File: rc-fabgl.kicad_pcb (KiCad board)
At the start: 2 copper layers, 99.1 x 49.9 mm, 45 parts, among them J1 RC2014, J2 RC2014_Enh, J3 Serial, J5 Keyboard, J6 VGA, Q1 2N7000, Q2 2N7000, SW1 Reset, SW2 Boot, U1 MCP1825S, U2 ESP32-WROVER-E, U3 74LVC125

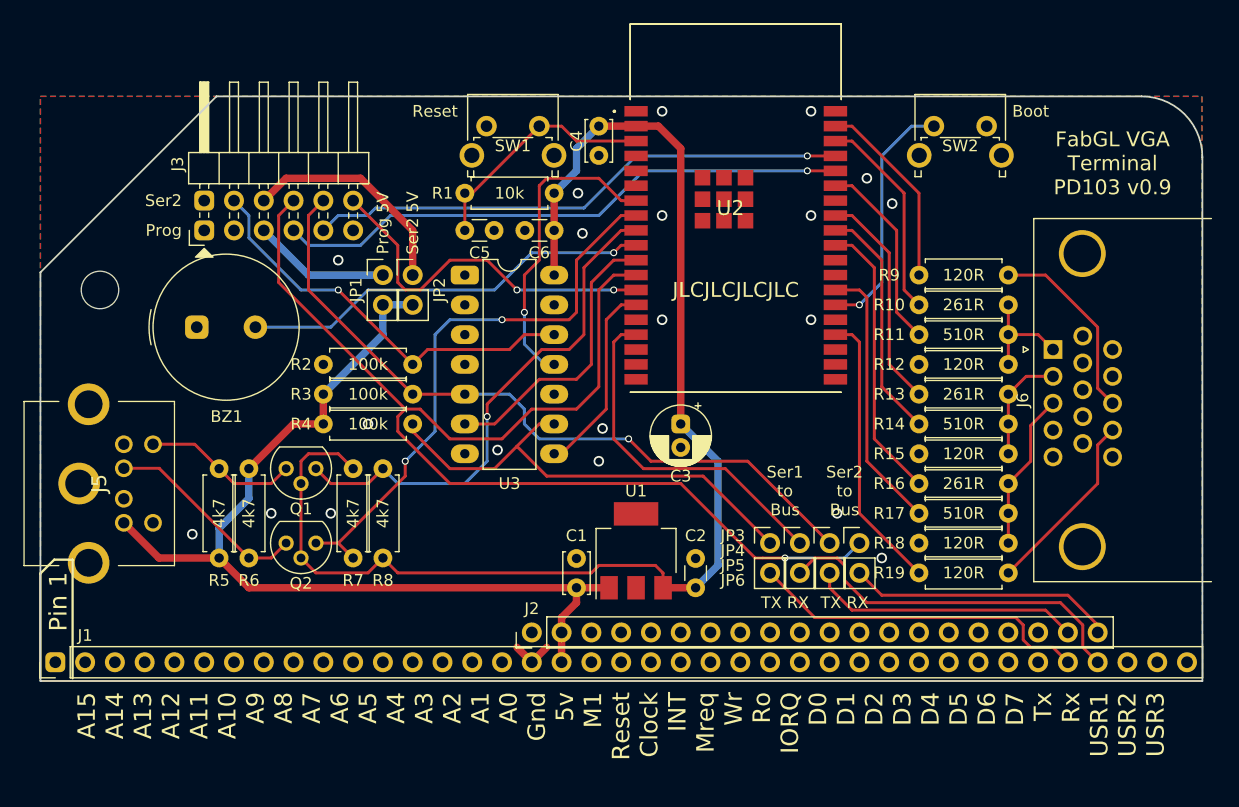
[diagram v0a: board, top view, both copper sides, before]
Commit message: Fixed component references, footprint 3D paths
Fixed component references, and corrected footprint 3D model paths. Changed serial headers to single right-angle part.
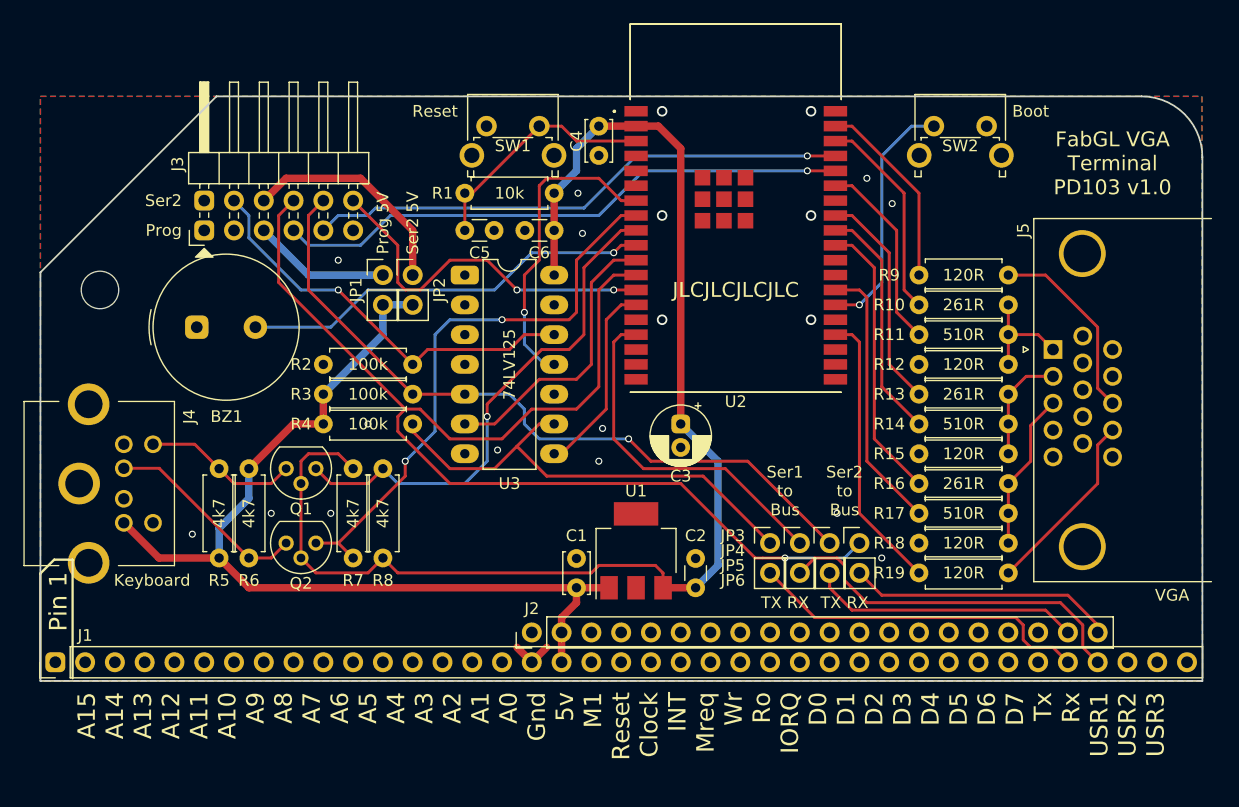
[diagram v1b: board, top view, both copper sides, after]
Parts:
- removed J6: VGA, rc-fabgl:DSUB-15-HD_Female_Horizontal_P2.29x2.54mm_Housed
- added J4: Keyboard, rc-fabgl:Mini-DIN-6-Socket, F.Cu at (159.5, 133.3)
- J5: value Keyboard -> VGA; footprint rc-fabgl:Mini-DIN-6-Socket -> rc-fabgl:DSUB-15-HD_Female_Horizontal_P2.29x2.54mm_Housed
- U3: value 74LVC125 -> 74LV125
- moved J5 79.9 mm to (238.8, 123.2)
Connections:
- J5 pad 1: /KBDat_5v -> /Red
- J5 pad 2: Net-(J5-Pad2) -> /Grn
- J5 pad 3: GND -> /Blu
- J5 pad 4: +5V -> Net-(J5-Pad4)
- J5 pad 5: /KBClk_5V -> GND
- J5 pad 6: Net-(J5-Pad6) -> GND
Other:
- board text added: "FabGL VGA Terminal PD103 v1.0"
- board text removed: "FabGL VGA Terminal PD103 v0.9"

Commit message: Move ESP32 pads outward
Move ESP32 pads outward to ease hand-soldering and alleviate under-module solder spills
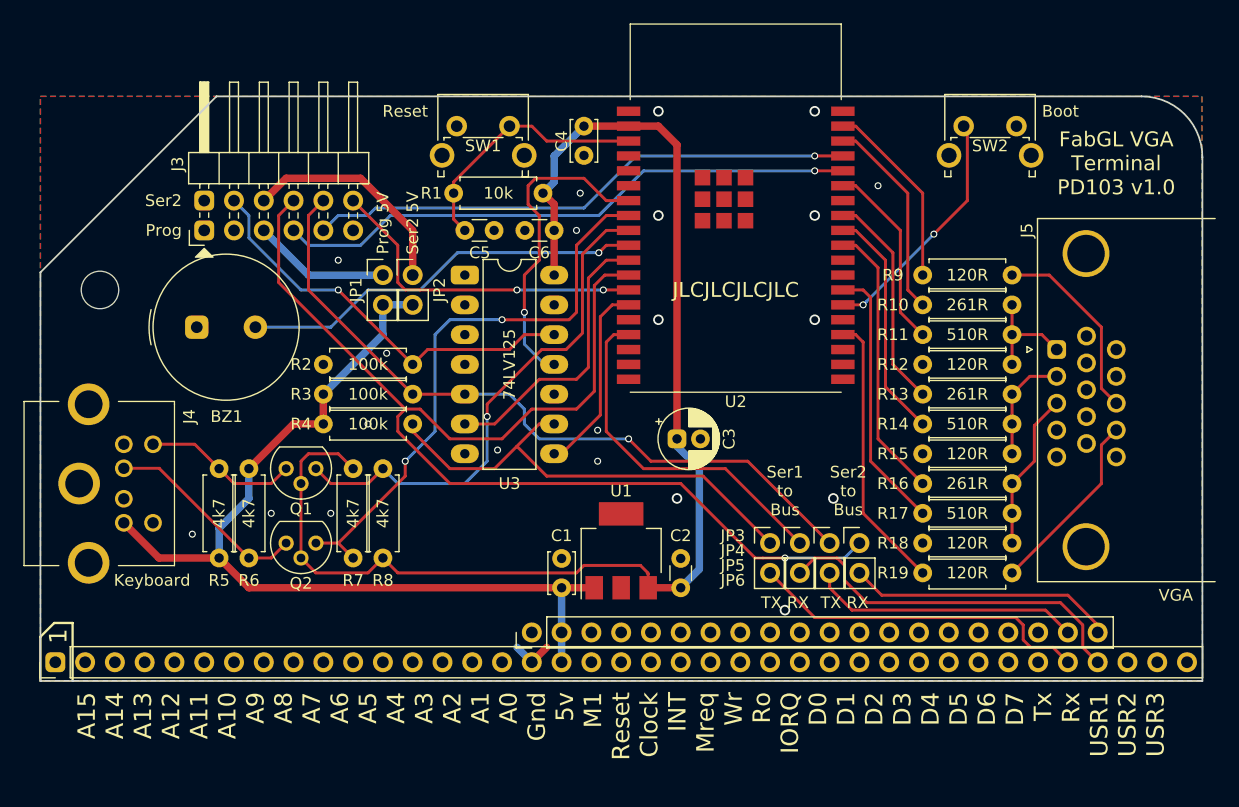
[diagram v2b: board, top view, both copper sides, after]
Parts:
- moved SW1 2.54 mm to (187.9, 104.1)
- moved SW2 2.54 mm to (231.1, 104.1)
- moved C3 1.31 mm to (206.7, 130.8), turned to 0 degrees
- moved C1 1.27 mm to (196.8, 143.5)
- moved C2 1.27 mm to (207.0, 143.5)
- moved C4 1.27 mm to (198.8, 104.1)
- moved U1 1.27 mm to (201.9, 140.4)
- moved R1 0.95 mm to (195.3, 109.9)
- moved J5 0.32 mm to (239.1, 123.2)
- moved R10 0.32 mm to (227.6, 119.4)
- moved R11 0.32 mm to (227.6, 121.9)
- moved R12 0.32 mm to (227.6, 124.5)
- moved R13 0.32 mm to (227.6, 127.0)
- moved R14 0.32 mm to (227.6, 129.5)
- moved R15 0.32 mm to (227.6, 132.1)
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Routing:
- net Ser2RTS: track 31.3 -> 28.5 mm
- net +5V: track 82.0 -> 80.2 mm
- net /Reset: track 20.7 -> 21.9 mm
- net Ser2CTS_3V: track 27.2 -> 27.9 mm
- net /ProgTX: track 46.3 -> 46.9 mm
- net /ProgRX: track 49.4 -> 50.0 mm
- net /Bell: track 35.4 -> 34.7 mm
- net /Boot: track 21.0 -> 20.8 mm, vias 1 -> 2
- net GND: vias 20 -> 21
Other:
- board text added: "1"
- board text added: "FabGL Terminal PD103 v1.0"
- board text removed: "Pin 1"

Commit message: Tidy up silkscreen
Tidy up silkscreen, update gerbers
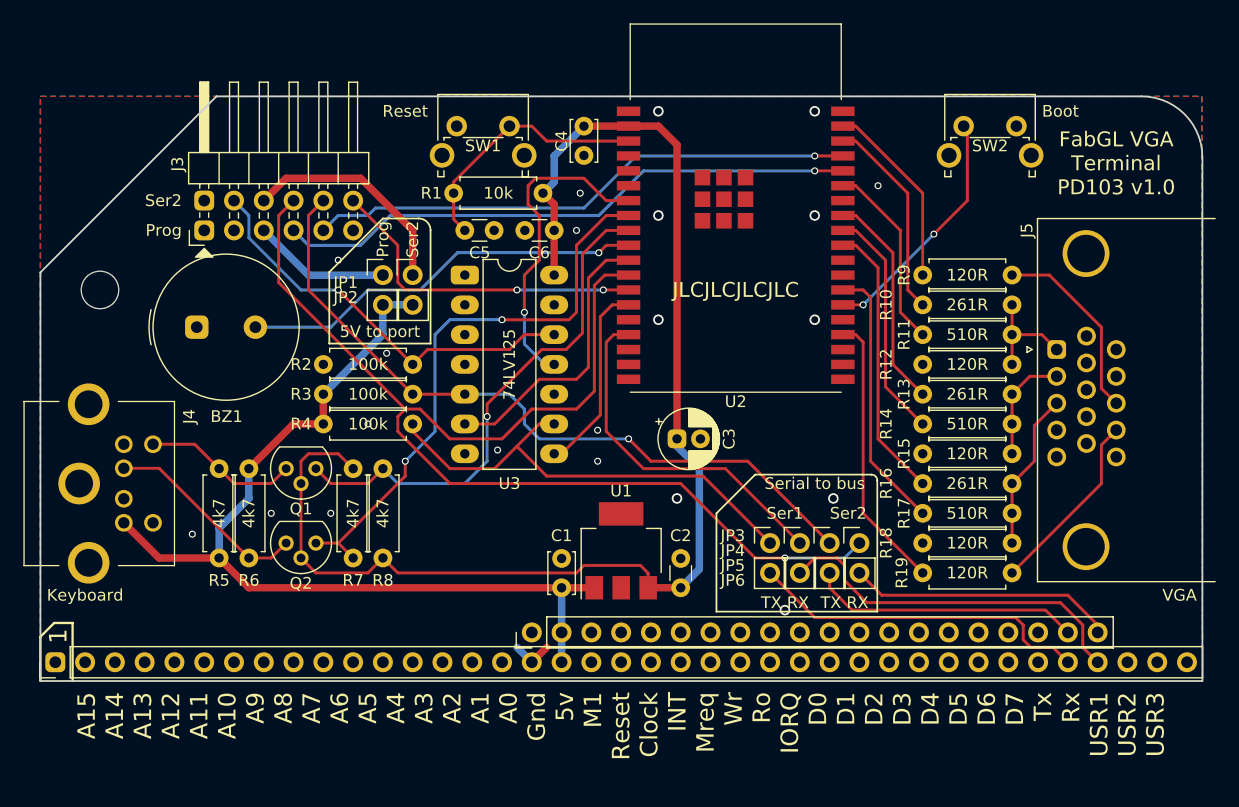
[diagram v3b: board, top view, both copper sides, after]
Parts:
- JP1: value Prog 5V -> Prog
- JP2: value Ser2 5V -> Ser2
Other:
- board text added: "5V to port"
- board text added: "Ser1"
- board text added: "Serial to bus"
- board text removed: "Ser1 to Bus"
- board text removed: "Ser2 to Bus"

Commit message: Fix strapping pin issue - isolate Ser1 during reset
Used spare buffer to invert and delay reset signal, used that to disable Ser1 during reset. This prevents GPIO12 from setting the flash/PSRAM voltage incorrectly. Keyboard footprint was reversed (thanks for nothing SamacSys!)
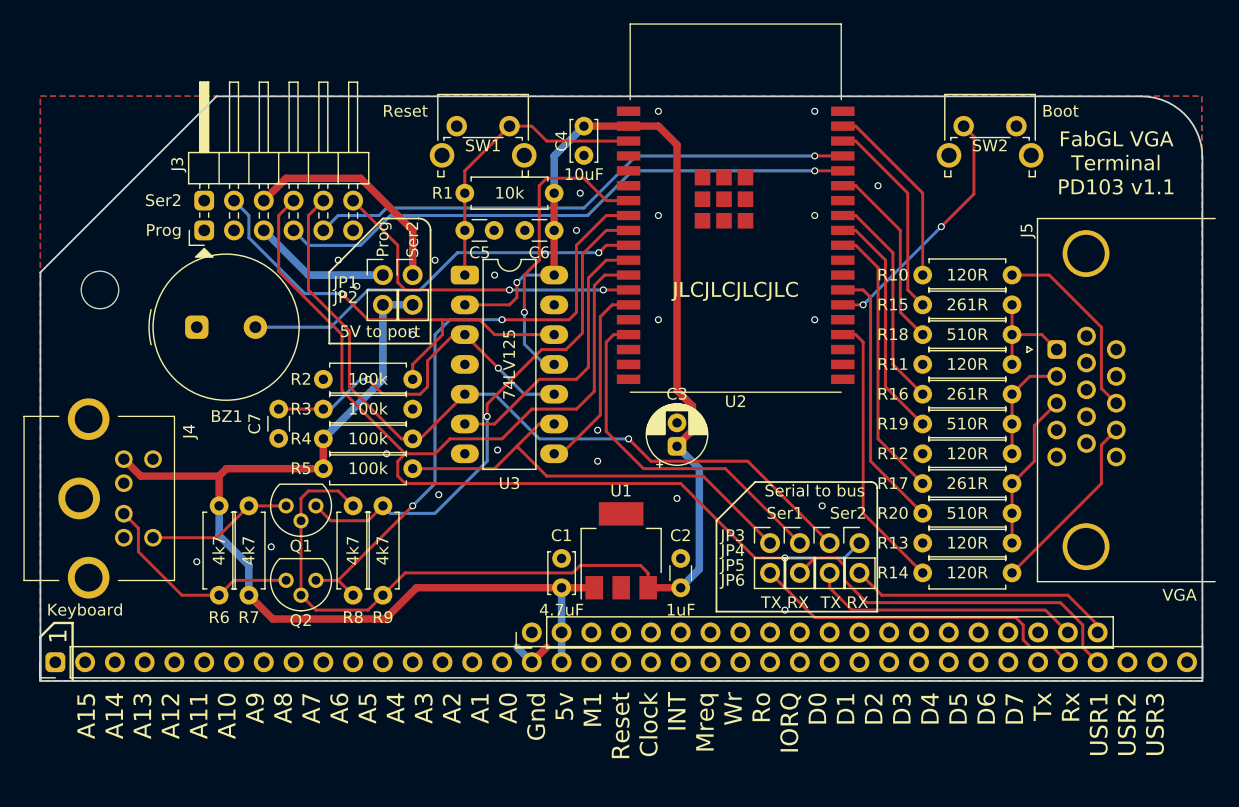
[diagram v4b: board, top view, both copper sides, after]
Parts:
- removed the R19 at (227.6, 142.2)
- removed the R4 at (176.5, 129.5)
- added C7: 0.1uF, Capacitor_THT:C_Disc_D3.0mm_W1.6mm_P2.50mm, F.Cu at (172.7, 130.8)
- added R14: 120R, Resistor_THT:R_Axial_DIN0207_L6.3mm_D2.5mm_P7.62mm_Horizontal, F.Cu at (227.6, 142.2)
- added R3: 100k, Resistor_THT:R_Axial_DIN0207_L6.3mm_D2.5mm_P7.62mm_Horizontal, F.Cu at (176.5, 128.3)
- added R5: 100k, Resistor_THT:R_Axial_DIN0207_L6.3mm_D2.5mm_P7.62mm_Horizontal, F.Cu at (176.5, 133.3)
- BZ1: value Bell -> Buzzer
- C3: value 10uF -> 22uF
- moved R6 4.07 mm to (167.6, 136.5)
- moved R7 4.07 mm to (170.2, 144.1)
- moved R4 3.81 mm to (176.5, 130.8)
- moved Q1 3.18 mm to (175.9, 136.5)
- moved Q2 3.18 mm to (175.9, 142.9)
- moved R8 3.18 mm to (179.1, 136.5)
- moved R9 3.18 mm to (181.6, 144.1)
- moved J4 1.27 mm to (159.5, 134.6)
- moved R2 1.27 mm to (176.5, 125.7)
- moved R1 0.95 mm to (196.2, 109.9)
- moved C3 0.63 mm to (206.7, 131.4), turned to 90 degrees
- renumbered R9 to R10, R12 to R11, R15 to R12, R18 to R13, R10 to R15, R13 to R16, R16 to R17, R11 to R18, R14 to R19, R17 to R20, R3 to R4, R5 to R7, R7 to R8, R8 to R9
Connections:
- net /Bell renamed /Buzz
- C5 pad 1: /Reset -> ~Reset
- R1 pad 2: /Reset -> ~Reset
- SW1 pad 2: /Reset -> ~Reset
- U2 pad 3: /Reset -> ~Reset
- U3 pad 1: GND -> ~Reset
- U3 pad 10: GND -> /~BufEn
- U3 pad 2: GND -> +3V3
- U3 pad 3: Net-(U3-Pad3) -> /~BufEn
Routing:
- net /~BufEn: track 0.00 -> 30.6 mm, vias 0 -> 2
- net ~Reset: track 0.00 -> 25.0 mm
- net /Reset: track 21.9 -> 0.00 mm
- net +3V3: track 111.7 -> 121.7 mm, vias 0 -> 1
- net /Ser2RX_5V: track 62.3 -> 67.5 mm
- net +5V: track 80.2 -> 84.8 mm
- net /Ser2CTS_5V: track 35.3 -> 39.3 mm
- net KBDat_3V: track 49.0 -> 52.1 mm
- net /Ser1RX_5V: track 40.6 -> 38.7 mm
- net Ser2TX: track 100.5 -> 102.2 mm
- net Ser2CTS_3V: track 27.9 -> 26.6 mm
- net /KBDat_5v: track 17.5 -> 18.4 mm
- net /KBClk_5V: track 13.3 -> 12.5 mm
- net KBClk_3V: track 44.0 -> 44.8 mm
- net GND: track 3.59 -> 3.64 mm, vias 21 -> 24
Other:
- board text added: "FabGL Terminal PD103 v1.1"
- board text added: "FabGL VGA Terminal PD103 v1.1"
- board text removed: "FabGL Terminal PD103 v1.0"
- board text removed: "FabGL VGA Terminal PD103 v1.0"
